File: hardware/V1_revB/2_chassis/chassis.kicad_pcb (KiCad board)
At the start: 2 copper layers, 39.1 x 31.7 mm, 18 parts, among them J7 , SW2 , SW3 NKK_NR01

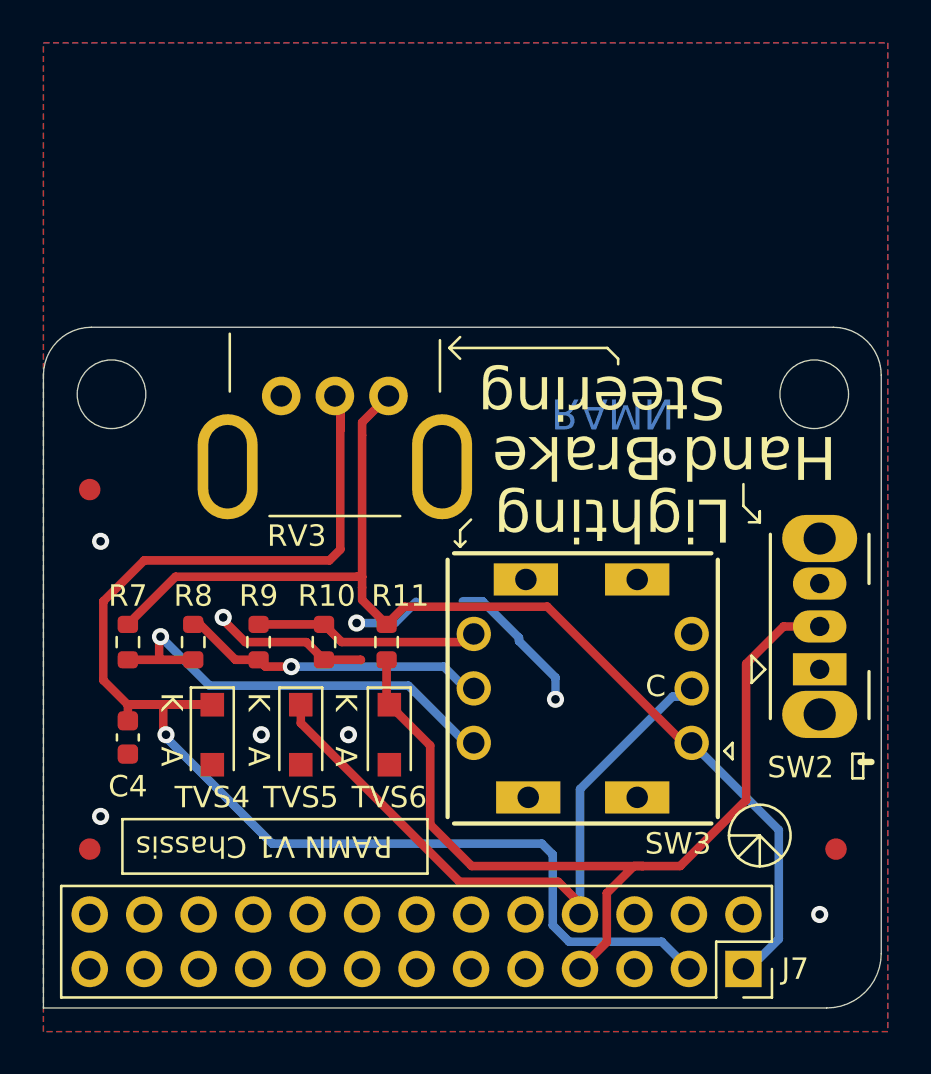
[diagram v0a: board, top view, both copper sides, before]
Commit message: feat: potentiometer footprint changed
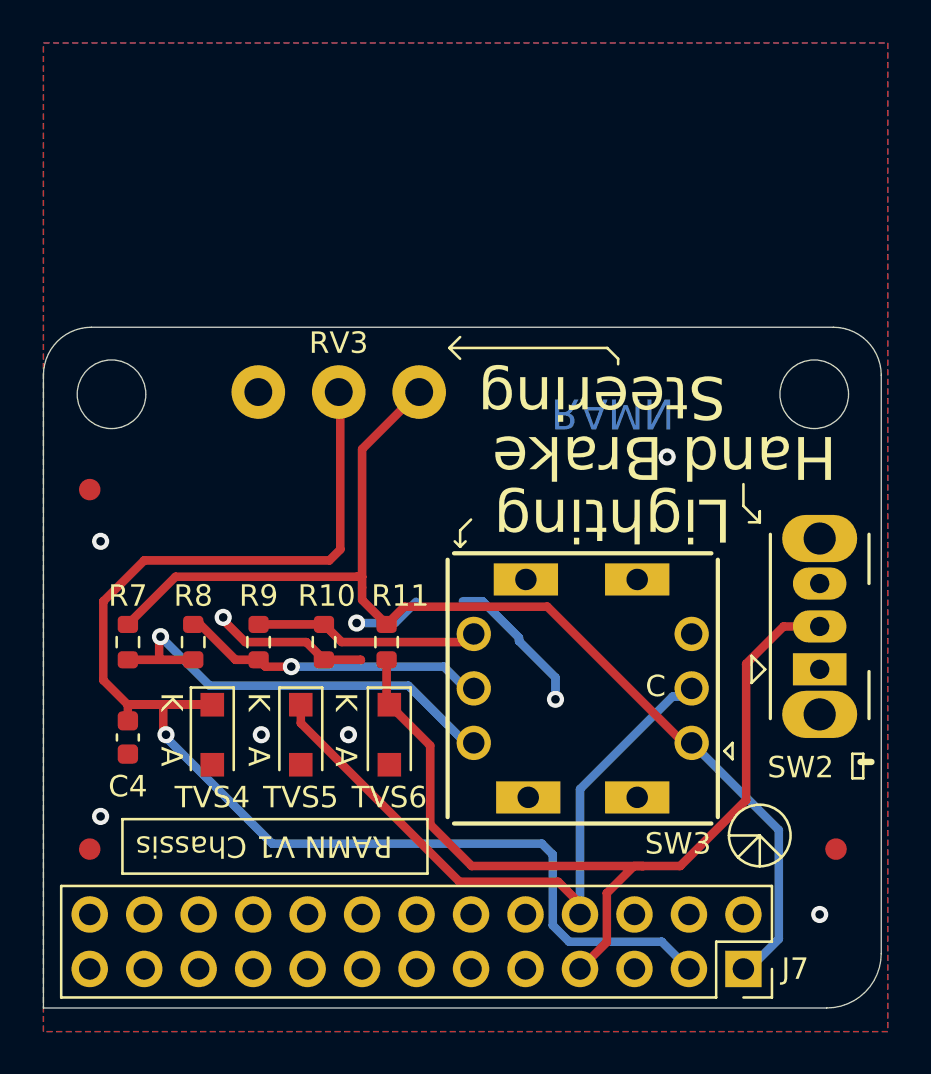
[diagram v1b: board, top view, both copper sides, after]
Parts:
- J7, SW2: value (none) -> ~
- RV3: value R_POT_TRIM_US -> POT_ECU; footprint custom:RK09K1110A2S -> Global_Library:POT_ECU
- moved RV3 2.82 mm to (45.9, 36.6), turned to 0 degrees
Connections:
- J7 pad 10: Net-(J7-Pad10) -> unconnected-(J7-Pin_10-Pad10)
- J7 pad 11: Net-(J7-Pad11) -> unconnected-(J7-Pin_11-Pad11)
- J7 pad 12: Net-(J7-Pad12) -> unconnected-(J7-Pin_12-Pad12)
- J7 pad 13: Net-(J7-Pad13) -> unconnected-(J7-Pin_13-Pad13)
- J7 pad 14: Net-(J7-Pad14) -> unconnected-(J7-Pin_14-Pad14)
- J7 pad 15: Net-(J7-Pad15) -> unconnected-(J7-Pin_15-Pad15)
- J7 pad 16: Net-(J7-Pad16) -> unconnected-(J7-Pin_16-Pad16)
- J7 pad 17: Net-(J7-Pad17) -> unconnected-(J7-Pin_17-Pad17)
- J7 pad 18: Net-(J7-Pad18) -> unconnected-(J7-Pin_18-Pad18)
- J7 pad 19: Net-(J7-Pad19) -> unconnected-(J7-Pin_19-Pad19)
- J7 pad 20: Net-(J7-Pad20) -> unconnected-(J7-Pin_20-Pad20)
- J7 pad 21: Net-(J7-Pad21) -> unconnected-(J7-Pin_21-Pad21)
- J7 pad 22: Net-(J7-Pad22) -> unconnected-(J7-Pin_22-Pad22)
- J7 pad 23: Net-(J7-Pad23) -> unconnected-(J7-Pin_23-Pad23)
- J7 pad 24: Net-(J7-Pad24) -> unconnected-(J7-Pin_24-Pad24)
- J7 pad 25: Net-(J7-Pad25) -> unconnected-(J7-Pin_25-Pad25)
- J7 pad 26: Net-(J7-Pad26) -> unconnected-(J7-Pin_26-Pad26)
- J7 pad 5: Net-(J7-Pad5) -> unconnected-(J7-Pin_5-Pad5)
- J7 pad 6: Net-(J7-Pad6) -> unconnected-(J7-Pin_6-Pad6)
- J7 pad 9: Net-(J7-Pad9) -> unconnected-(J7-Pin_9-Pad9)
- RV3 pad 1: /3V3_ECU -> GND
- RV3 pad 3: GND -> /3V3_ECU
- SW2 pad 1: Net-(SW2-Pad1) -> unconnected-(SW2-A-Pad1)
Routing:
- net Wheel: track 67.3 -> 66.3 mm
- net /3V3_ECU: track 53.7 -> 54.5 mm
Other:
- net class Default removed
